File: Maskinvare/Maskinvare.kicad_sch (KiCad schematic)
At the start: 22 parts, among them J1 12V IN, J2 I2C connector, J3 Error interrupt connector, M1 Fan 0, M2 Fan 1, Q1 IR phototransistor, Q2 Q_Photo_NPN, U1 AVR128DA48 CURIOSITY NANO, U2 L7805

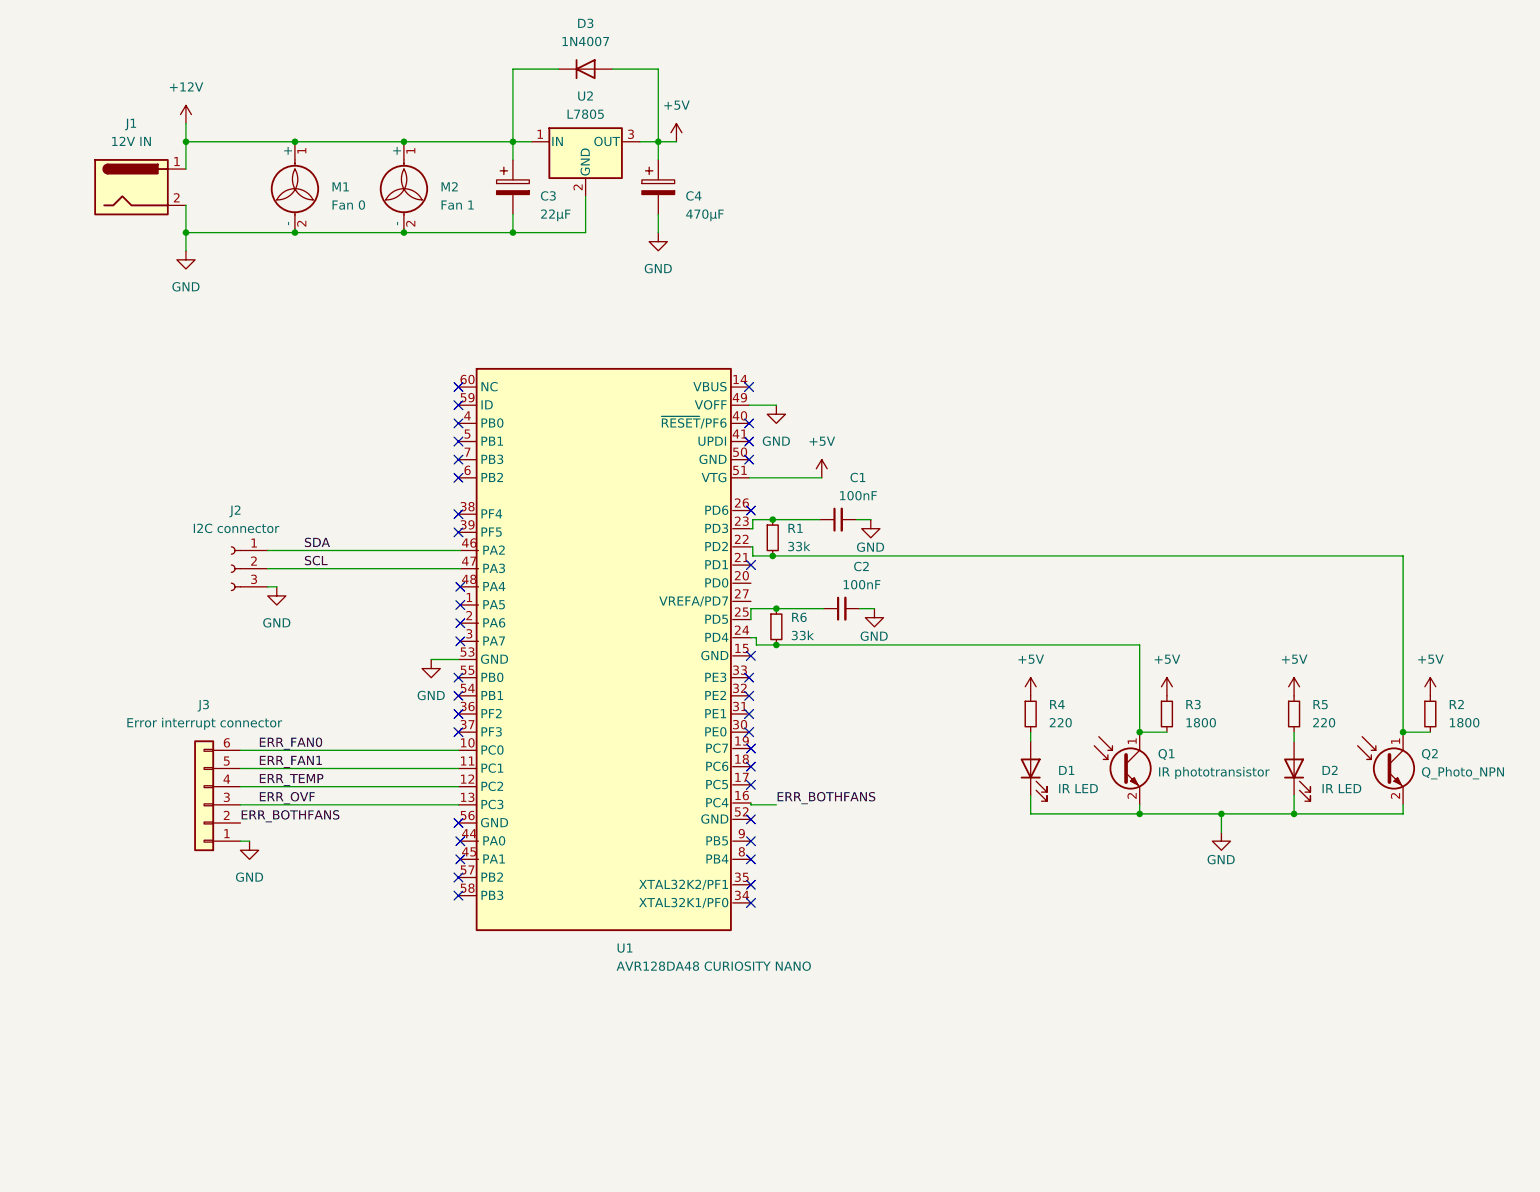
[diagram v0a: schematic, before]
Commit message: Updated pin position for external voltage measurement, added functionality for both fans error.
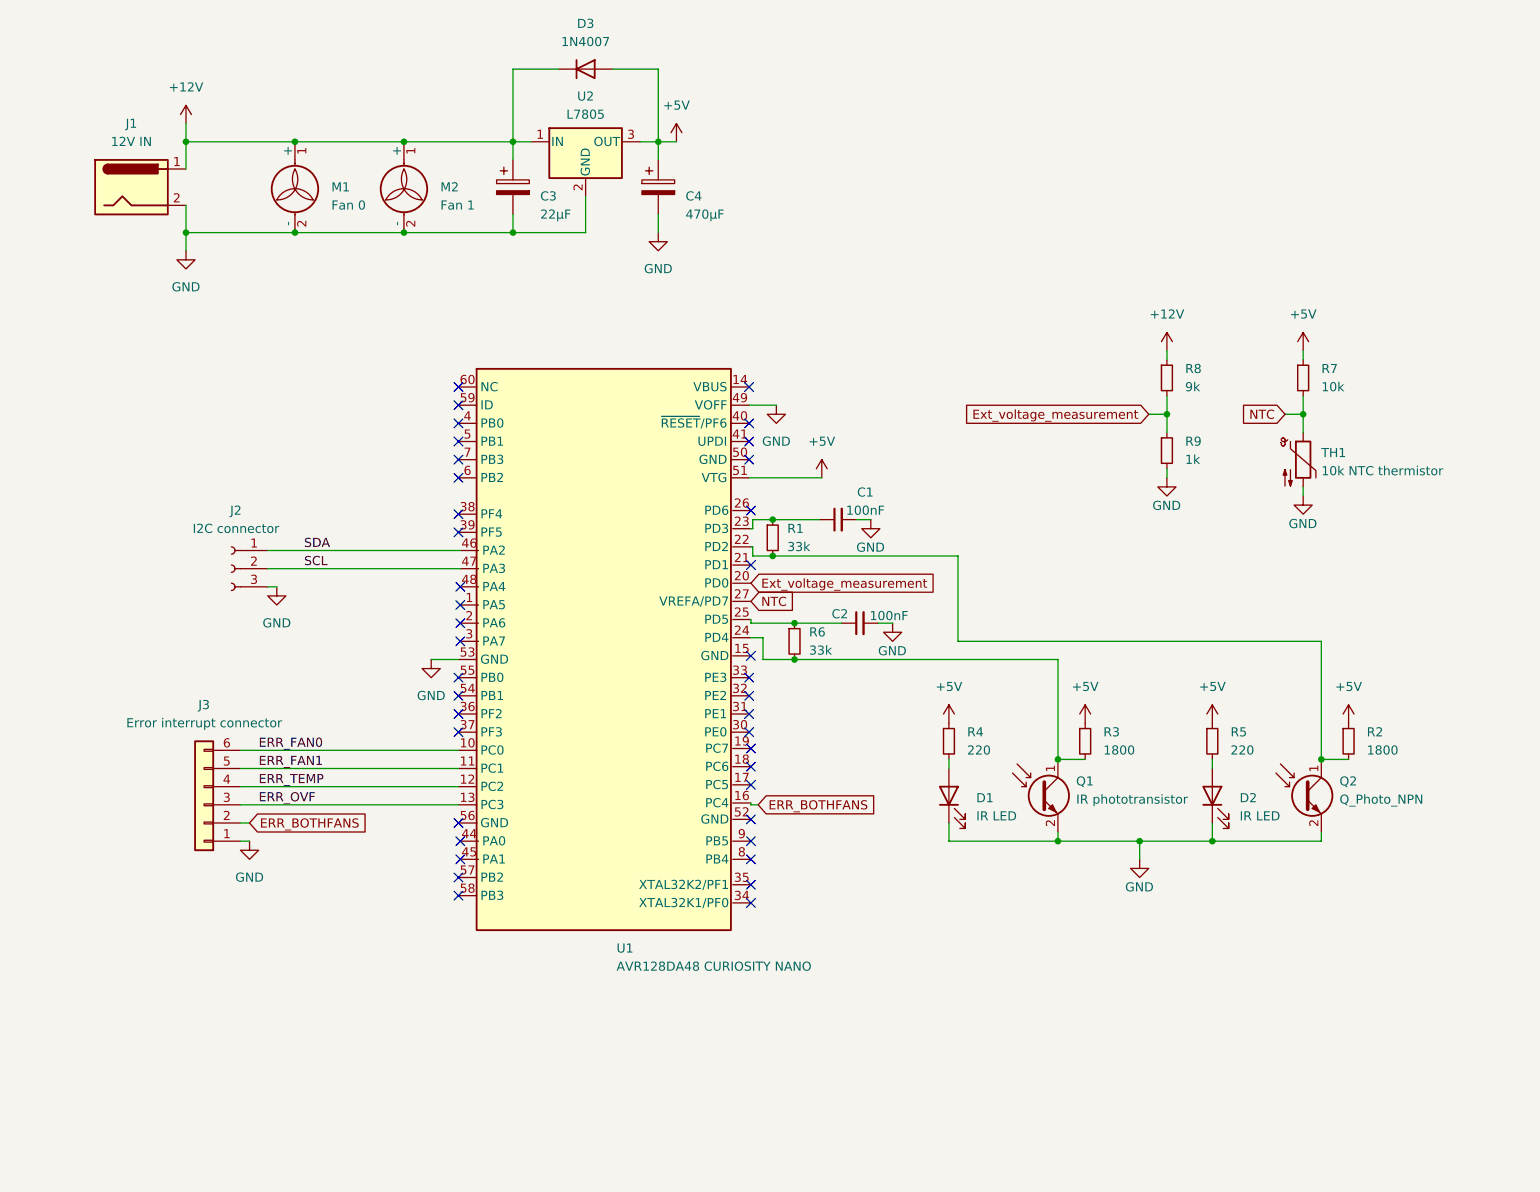
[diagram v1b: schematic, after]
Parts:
- added R7: 10k, symbol Device:R_Small
- added R8: 9k, symbol Device:R_Small
- added R9: 1k, symbol Device:R_Small
- added TH1: 10k NTC thermistor, symbol Device:Thermistor_NTC
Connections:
- net +12V: now also R8.1
- net +5V: now also R7.1
- net GND: now also R9.2, TH1.2
- net Ext_voltage_measurement: now reaches U1.20 (PD0)
- net Ext_voltage_measurement: now also R8.2, R9.1
- net NTC: now reaches U1.27 (VREFA/PD7)
- net NTC: now also R7.2, TH1.1
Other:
- company: (none) -> Steinar og Henrik
- title: (none) -> Fan monitor
- moved on the sheet: C2, D1, D2, Q1, Q2, R2, R3, R4, R5, R6

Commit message: Forgot to push some comments before delivering the assignment, whoops
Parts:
- added D4, D5, D6, D7, D8: Red LED, symbol Device:LED
- added R10, R11, R12, R13, R14: 2k, symbol Device:R_Small
- J2: value I2C connector -> I2C connections
- J3: value Error interrupt connector -> Error interrupt connections
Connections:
- net ERR_BOTHFANS: now also R14.1
- net ERR_FAN0: now also R10.1
- net ERR_FAN1: now also R11.1
- net ERR_OVF: now also R13.1
- net ERR_TEMP: now also R12.1
- net GND: now also D4.1 (K), D5.1 (K), D6.1 (K), D7.1 (K), D8.1 (K)
- new net: D6.2 (A), R12.2
- new net: D4.2 (A), R10.2
- new net: D7.2 (A), R13.2
- new net: D5.2 (A), R11.2
- new net: D8.2 (A), R14.2
